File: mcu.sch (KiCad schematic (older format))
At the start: 31 parts, among them J4 UEXT, P1 CONN_01X02, SW2 SW_PUSH, T3 MMBT3904, U2 STM32F072CB, U6 24AA01, Y1 8MHz

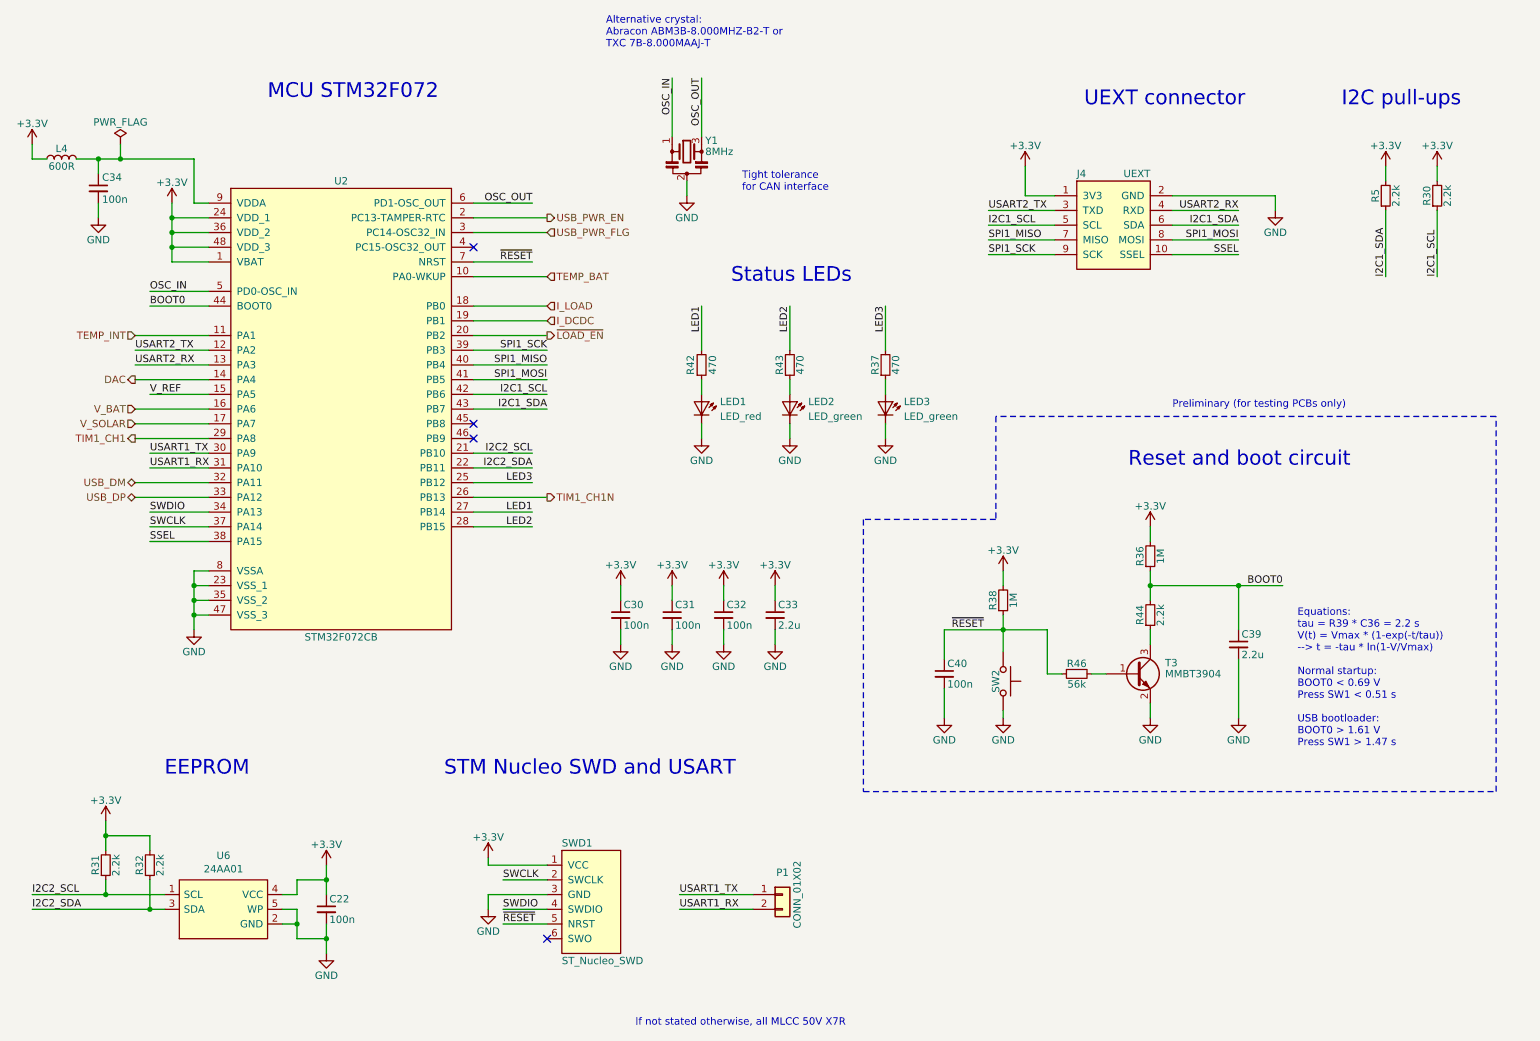
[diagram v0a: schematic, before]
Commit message: Several improvements (v0.4) after first tests
- Ultra-low-power MCU STM32L072
- Larger screw terminals
- USB power supply replaced by more efficient SMPS
- High-side load switch with P-MOS
- High-side current measurement to include USB current in load measurement
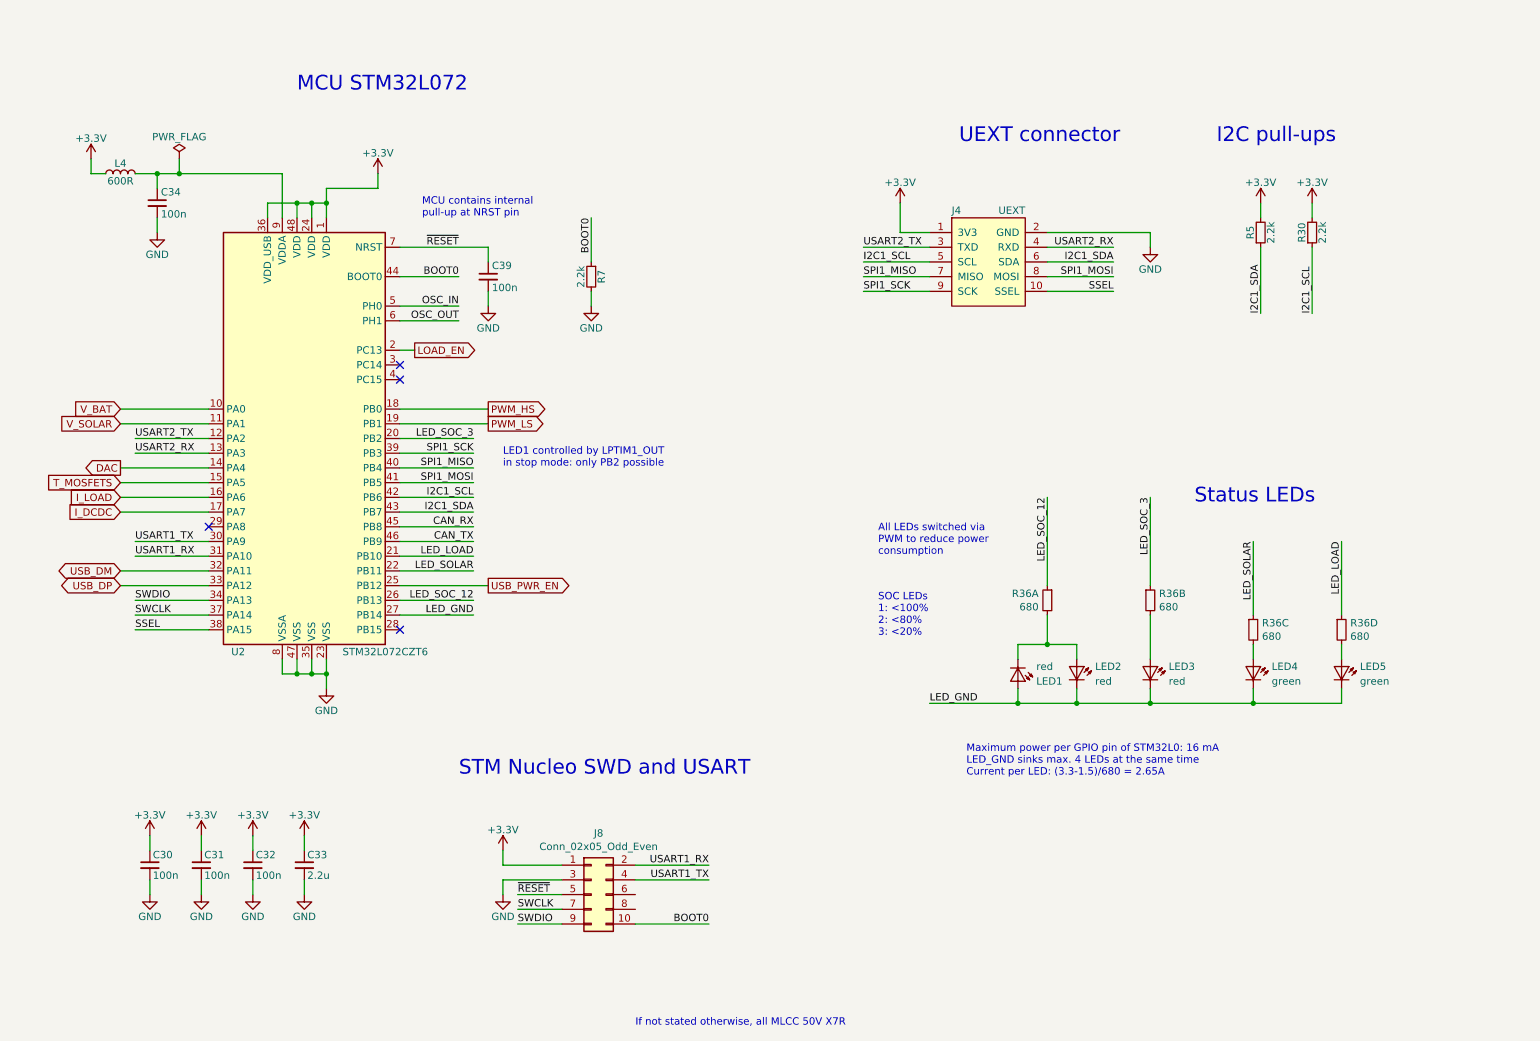
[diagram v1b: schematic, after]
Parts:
- removed C22, C40: 100n, LibreSolar:C_0603_1608, symbol Project:C
- removed P1: CONN_01X02, Connector_PinHeader_2.54mm:PinHeader_1x02_P2.54mm_Vertical, symbol Connector_Generic:Conn_01x02
- removed R31, R32, R44: 2.2k, LibreSolar:R_0603_1608, symbol Project:R
- removed R36, R38: 1M, LibreSolar:R_0603_1608, symbol Project:R
- removed R37, R42, R43: 470, LibreSolar:R_0603_1608, symbol Project:R
- removed R46: 56k, LibreSolar:R_0603_1608, symbol Project:R
- removed SW2: SW_PUSH, LibreSolar:SW_SPST_6mm, symbol Switch:SW_Push
- removed SWD1: ST_Nucleo_SWD, Connector_PinHeader_2.54mm:PinHeader_1x06_P2.54mm_Vertical, symbol Project:ST_Nucleo_SWD
- removed T3: MMBT3904, LibreSolar:SOT-23, symbol Transistor_BJT:BC817
- removed U2: STM32F072CB, Package_QFP:LQFP-48_7x7mm_P0.5mm, symbol Project:STM32F072CB
- removed U6: 24AA01, LibreSolar:SOT-23-5, symbol Project:24AA01
- removed Y1: 8MHz, LibreSolar:Resonator_Murata_CSTCE_G, symbol Device:Resonator_Small
- added J8: Conn_02x05_Odd_Even, Connector_PinHeader_2.54mm:PinHeader_2x05_P2.54mm_Vertical, symbol Connector_Generic:Conn_02x05_Odd_Even
- added LED2, LED3: red, LED_SMD:LED_0603_1608Metric, symbol Project:D_LED
- added R36: 680, LibreSolar:R_Array_Convex_4x0603, symbol Project:R_Array_4
- added R7: 2.2k, LibreSolar:R_0603_1608, symbol Project:R
- added U2: STM32L072CZT6, Package_QFP:LQFP-48_7x7mm_P0.5mm, symbol MCU_ST_STM32L0:STM32L072CZTx
- C39: value 2.2u -> 100n; Manufacturer Murata -> Yageo; PartNumber GRM188R61E225KA12D -> CC0603KRX7R9BB104; Remarks 25V, X5R -> (none)
- LED1: value LED_red -> red; Remarks red -> (none)
- LED2: value LED_green -> green; PartNumber LTST-C190GKT -> LTST-C190KGKT
- LED5: renamed from LED3; value LED_green -> green; PartNumber LTST-C190GKT -> LTST-C190KGKT
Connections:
- net +3V3: now also J8.1 (Pin_1), U2.1 (VDD), U2.24 (VDD), U2.36 (VDD_USB), U2.48 (VDD)
- net BOOT0: now also J8.10 (Pin_10), R7.1, U2.44 (BOOT0); no longer C39.1
- net DAC: now also U2.14 (PA4)
- net GND: now also J8.3 (Pin_3), R7.2, U2.23 (VSS), U2.35 (VSS), U2.47 (VSS), U2.8 (VSSA); no longer LED1.1 (K), LED2.1 (K), LED5.1 (K)
- net I2C1_SCL: now also U2.42 (PB6)
- net I2C1_SDA: now also U2.43 (PB7)
- net I_DCDC: now also U2.17 (PA7)
- net I_LOAD: now also U2.16 (PA6)
- net OSC_IN: now also U2.5 (PH0)
- net OSC_OUT: now also U2.6 (PH1)
- net SPI1_MISO: now also U2.40 (PB4)
- net SPI1_MOSI: now also U2.41 (PB5)
- net SPI1_SCK: now also U2.39 (PB3)
- net SSEL: now also U2.38 (PA15)
- net SWCLK: now also J8.7 (Pin_7), U2.37 (PA14)
- net SWDIO: now also J8.9 (Pin_9), U2.34 (PA13)
- net USART1_RX: now also J8.2 (Pin_2), U2.31 (PA10)
- net USART1_TX: now also J8.4 (Pin_4), U2.30 (PA9)
- net USART2_RX: now also U2.13 (PA3)
- net USART2_TX: now also U2.12 (PA2)
- net USB_DM: now also U2.32 (PA11)
- net USB_DP: now also U2.33 (PA12)
- net USB_PWR_EN: now also U2.25 (PB12)
- net V_BAT: now also U2.10 (PA0)
- net V_SOLAR: now also U2.11 (PA1)
- net ~RESET: now also C39.1, J8.5 (Pin_5), U2.7 (NRST)
- net at C34.1, L4.2: now also U2.9 (VDDA)
- net LED_GND: now reaches LED1.2 (A)
- net LED_GND: now also LED2.1 (K), LED5.1 (K), LED2.1 (K), LED3.1 (K), U2.27 (PB14)
- net at LED2.2 (A): now also R36.6
- net at LED5.2 (A): now also R36.8
- new net: LED1.1 (K), LED2.2 (A), R36.2
- new net: LED3.2 (A), R36.4
- new net CAN_RX: U2.45 (PB8)
- new net CAN_TX: U2.46 (PB9)
- new net LED_LOAD: R36.7, U2.21 (PB10)
- new net LED_SOC_12: R36.1, U2.26 (PB13)
- new net LED_SOC_3: R36.3, U2.20 (PB2)
- new net LED_SOLAR: R36.5, U2.22 (PB11)
- new net LOAD_EN: U2.2 (PC13)
- new net PWM_HS: U2.18 (PB0)
- new net PWM_LS: U2.19 (PB1)
- new net T_MOSFETS: U2.15 (PA5)
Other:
- note added: "All LEDs switched via\nPWM to reduce power\nconsumption"
- note added: "LED1 controlled by LPTIM1_OUT\nin stop mode: only PB2 possible"
- note added: "MCU STM32L072"
- note added: "MCU contains internal\npull-up at NRST pin"
- note added: "Maximum power per GPIO pin of STM32L0: 16 mA\nLED_GND sinks max. 4 LEDs at the same time\nCurrent per LED: (3.3-1.5)/680 = 2.65A"
- note added: "SOC LEDs\n1: <100%\n2: <80%\n3: <20%"
- note removed: "Alternative crystal: \nAbracon ABM3B-8.000MHZ-B2-T or\nTXC 7B-8.000MAAJ-T"
- note removed: "EEPROM"
- note removed: "Equations:\ntau = R39 * C36 = 2.2 s\nV(t) = Vmax * (1-exp(-t/tau))\n--> t = -tau * ln(1-V/Vmax)\n\nNormal startup:\nBOOT0 < 0.69 V\nPress SW1 < 0.51 s\n\nUSB bootloader:\nBOOT0 > 1.61 V\nPress SW1 > 1.47 s"
- note removed: "MCU STM32F072"
- note removed: "Preliminary (for testing PCBs only)"
- note removed: "Reset and boot circuit"
- note removed: "Tight tolerance\nfor CAN interface"
- moved on the sheet: C30, C31, C32, C33, C34, J4, L4, LED4, LED5, R30, R5

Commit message: Board shape adjusted and 6P6C connector added
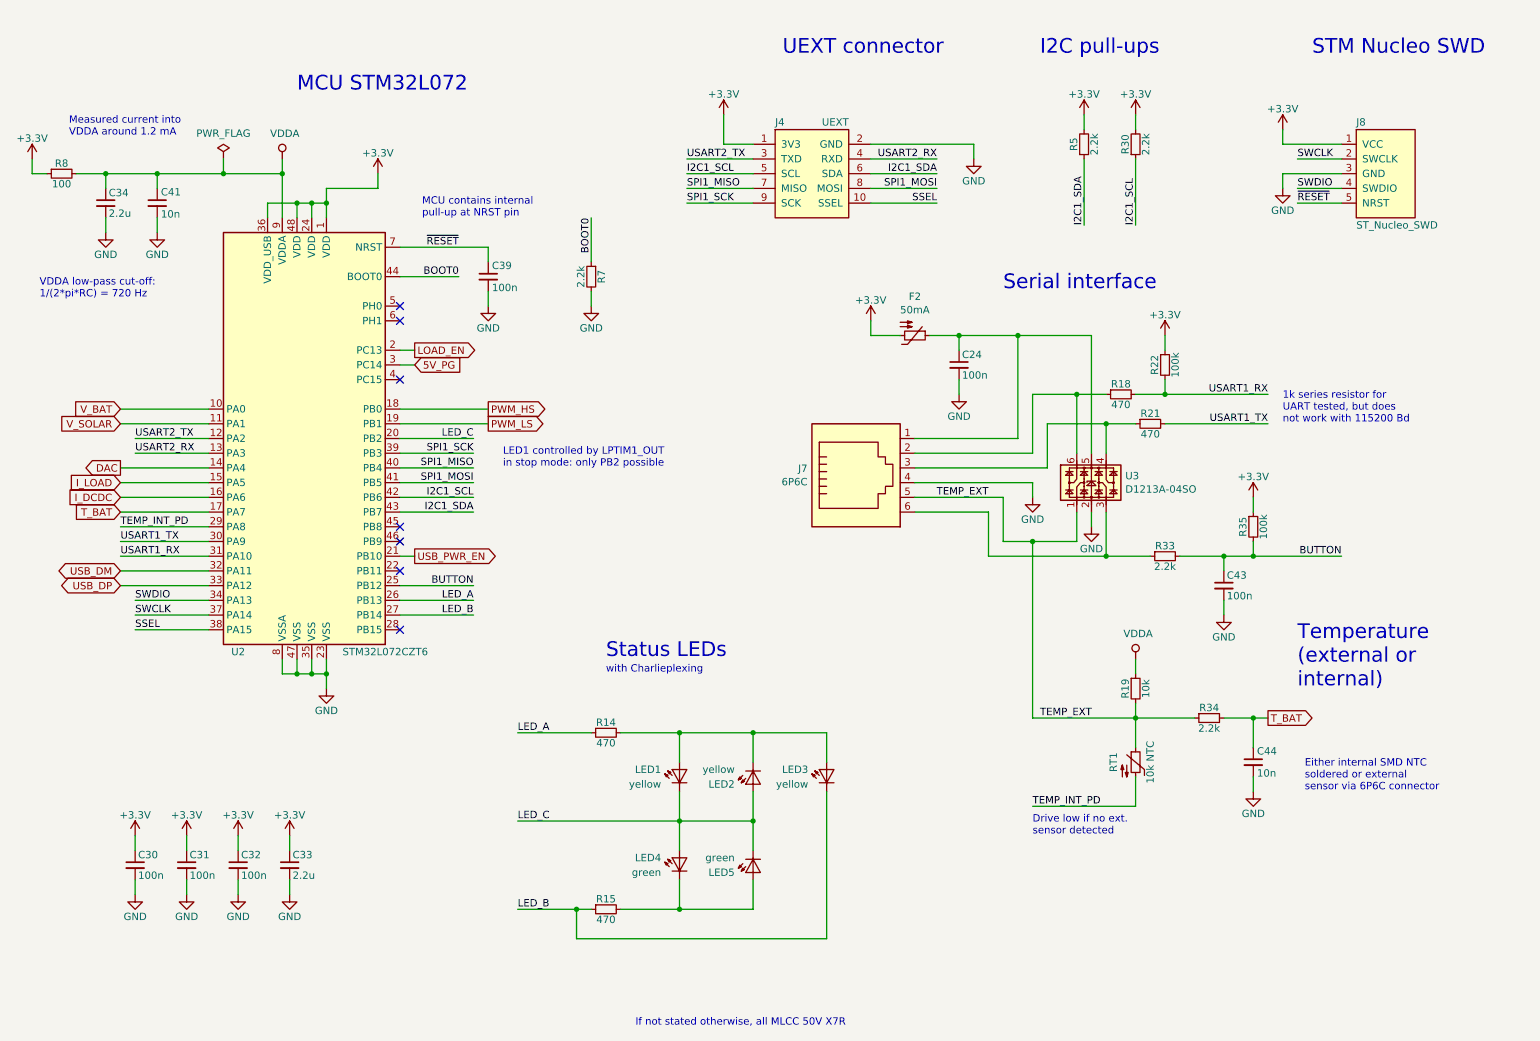
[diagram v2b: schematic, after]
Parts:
- removed J8: Conn_02x05_Odd_Even, Connector_PinHeader_2.54mm:PinHeader_2x05_P2.54mm_Vertical, symbol Connector_Generic:Conn_02x05_Odd_Even
- removed L4: 600R, Inductor_SMD:L_0603_1608Metric, symbol Project:L
- removed LED2: green, LED_SMD:LED_0603_1608Metric, symbol Project:D_LED
- removed LED2: red, LED_SMD:LED_0603_1608Metric, symbol Project:D_LED
- removed R36: 680, LibreSolar:R_Array_Convex_4x0603, symbol Project:R_Array_4
- added C24, C43: 100n, LibreSolar:C_0603_1608, symbol Project:C
- added C41, C44: 10n, LibreSolar:C_0603_1608, symbol Project:C
- added F2: 50mA, LibreSolar:R_1206_3216, symbol Project:R_PTC
- added J7: 6P6C, LibreSolar:RJ25_6P6C_TabUp, symbol Connector:6P6C
- added J8: ST_Nucleo_SWD, Connector_PinHeader_2.54mm:PinHeader_1x05_P2.54mm_Vertical, symbol Project:ST_Nucleo_SWD_5p
- added LED2: green, LibreSolar:LED_0603_D3.0mm, symbol Project:D_LED
- added LED2: yellow, LibreSolar:LED_0603_D3.0mm, symbol Project:D_LED
- added R14, R15, R18, R21: 470, LibreSolar:R_0603_1608, symbol Project:R
- added R19: 10k, LibreSolar:R_0603_1608, symbol Project:R
- added R22, R35: 100k, LibreSolar:R_0603_1608, symbol Project:R
- added R33, R34: 2.2k, LibreSolar:R_0603_1608, symbol Project:R
- added R8: 100, LibreSolar:R_0603_1608, symbol Project:R
- added RT1: 10k NTC, LibreSolar:R_0603_1608, symbol LibreSolar:R_NTC
- added U3: D1213A-04SO, LibreSolar:SOT-23-6, symbol Power_Protection:NUP4202
- C34: value 100n -> 2.2u; Manufacturer Yageo -> Murata; PartNumber CC0603KRX7R9BB104 -> GRM188R61E225KA12D; Remarks (none) -> 25V, X5R
- J4: Manufacturer (none) -> On Shore Technology Inc.; PartNumber (none) -> 302-S101
- LED1, LED3: value red -> yellow; footprint LED_SMD:LED_0603_1608Metric -> LibreSolar:LED_0603_D3.0mm; PartNumber LTST-C190KRKT -> LTST-C191KSKT; Remarks (none) -> Alternative: LTL-1CHY (3mm THT)
- LED5: footprint LED_SMD:LED_0603_1608Metric -> LibreSolar:LED_0603_D3.0mm; Remarks (none) -> Alternative: LTL-4231 (3mm THT)
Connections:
- net LED_LOAD is gone; now on net USB_PWR_EN: U2.21 (PB10)
- net LED_SOC_3 is gone; now on net LED_C: U2.20 (PB2)
- net T_MOSFETS is gone; now on net I_LOAD: U2.15 (PA5)
- net +3V3: now also F2.2, J8.1 (VCC), R22.1, R35.1, R8.1
- net GND: now also C24.2, C41.2, C43.2, C44.2, J7.4, J8.3 (GND), U3.2
- net I_DCDC: now also U2.16 (PA6); no longer U2.17 (PA7)
- net I_LOAD: no longer U2.16 (PA6)
- net SWCLK: now also J8.2 (SWCLK)
- net SWDIO: now also J8.4 (SWDIO)
- net USART1_RX: now also R18.2, R22.2
- net USART1_TX: now also R21.2
- net USB_PWR_EN: no longer U2.25 (PB12)
- net ~RESET: now also J8.5 (NRST)
- net VDDA: now reaches C34.1, U2.9 (VDDA)
- net VDDA: now also C41.1, R19.1, R8.2
- net at LED5.2 (A): now also LED2.1 (K), R15.2
- net LED_C: now reaches LED1.1 (K)
- net LED_C: now also LED5.1 (K), LED2.2 (A), LED2.2 (A)
- net at LED3.2 (A): now also LED1.2 (A), LED2.1 (K), R14.2
- net TEMP_INT_PD: now reaches U2.29 (PA8)
- net TEMP_INT_PD: now also RT1.2
- net 5V_PG: now reaches U2.3 (PC14)
- net CAN_RX: no longer names the net of U2.45 (PB8)
- net CAN_TX: no longer names the net of U2.46 (PB9)
- net LED_GND renamed LED_B
- net LED_B: now also R15.1; no longer LED1.2 (A), LED5.1 (K)
- net LED_SOC_12 renamed LED_A
- net LED_A: now also R14.1
- net LED_SOLAR: no longer names the net of U2.22 (PB11)
- net OSC_IN: no longer names the net of U2.5 (PH0)
- net OSC_OUT: no longer names the net of U2.6 (PH1)
- new net: C24.1, F2.1, J7.1, U3.5
- new net: J7.2, R18.1, U3.6
- new net: J7.3, R21.1, U3.4
- new net: J7.6, R33.1, U3.3
- new net BUTTON: C43.1, R33.2, R35.2, U2.25 (PB12)
- new net TEMP_EXT: J7.5, R19.2, R34.1, RT1.1, U3.1
- new net T_BAT: C44.1, R34.2, U2.17 (PA7)
- no-connect marks 4 -> 7
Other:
- note added: "1k series resistor for\nUART tested, but does \nnot work with 115200 Bd"
- note added: "Drive low if no ext. \nsensor detected"
- note added: "Either internal SMD NTC\nsoldered or external \nsensor via 6P6C connector"
- note added: "Measured current into\nVDDA around 1.2 mA"
- note added: "STM Nucleo SWD"
- note added: "Serial interface"
- note added: "Temperature\n(external or \ninternal)"
- note added: "VDDA low-pass cut-off:\n1/(2*pi*RC) = 720 Hz"
- note added: "with Charlieplexing"
- note removed: "All LEDs switched via\nPWM to reduce power\nconsumption"
- note removed: "Maximum power per GPIO pin of STM32L0: 16 mA\nLED_GND sinks max. 4 LEDs at the same time\nCurrent per LED: (3.3-1.5)/680 = 2.65A"
- note removed: "SOC LEDs\n1: <100%\n2: <80%\n3: <20%"
- note removed: "STM Nucleo SWD and USART"
- moved on the sheet: C30, C31, J4, LED1, LED3, LED5

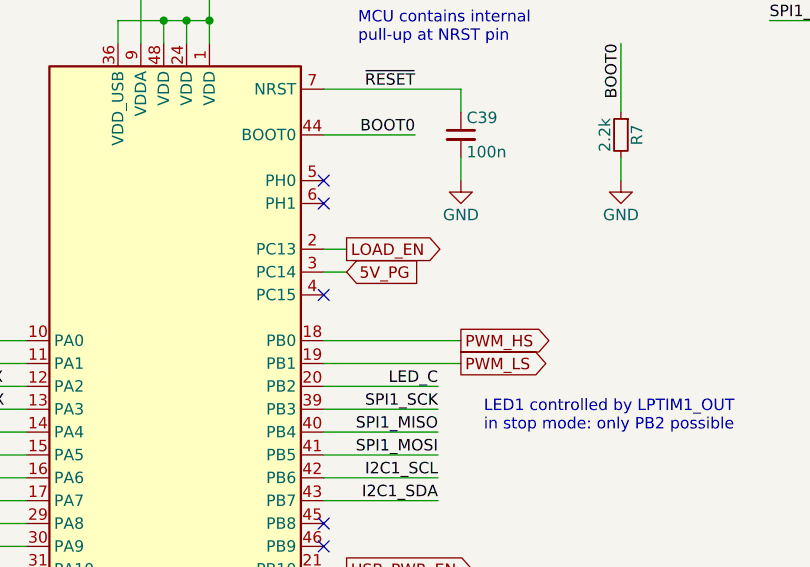
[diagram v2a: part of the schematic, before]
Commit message: Solar voltage input protection added
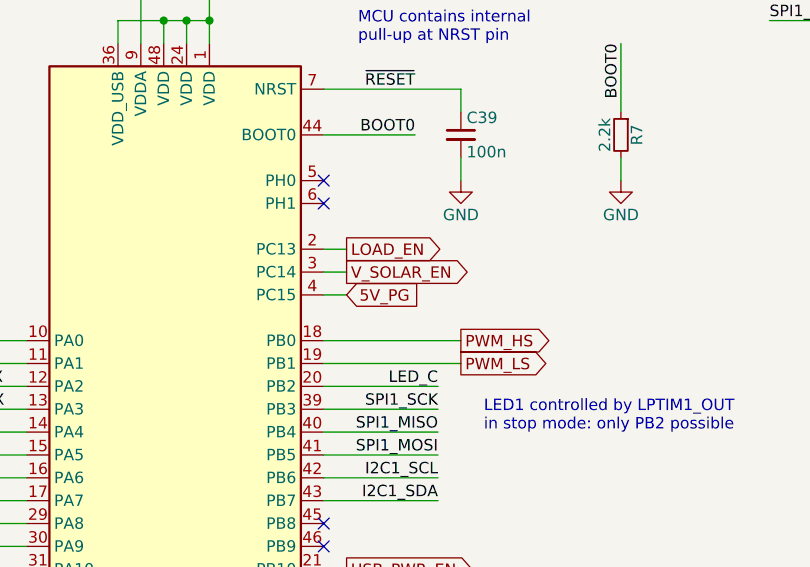
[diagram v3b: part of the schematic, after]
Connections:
- net 5V_PG: now also U2.4 (PC15); no longer U2.3 (PC14)
- new net V_SOLAR_EN: U2.3 (PC14)
- no-connect marks 7 -> 6
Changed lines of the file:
@@
 EESchema Schematic File Version 4
-LIBS:mptt-10a-cache
+LIBS:mppt-10a-cache
 EELAYER 29 0
 EELAYER END
@@
 Sheet 3 4
 Title "10A MPPT Charge Controller with USB"
-Date "2019-03-24"
-Rev "0.5"
+Date "2019-04-09"
+Rev "0.6"
 Comp "Libre Solar / Connected Energy"
 Comment1 "Author: Martin Jäger"
@@
 Wire Wire Line
 	2200 3900 1600 3900
-NoConn ~ 3500 3200
 Wire Wire Line
 	2200 4000 1600 4000
@@
 Wire Wire Line
 	3500 3100 3600 3100
-Text GLabel 3600 3100 2    50   Input ~ 0
+Text GLabel 3600 3200 2    50   Input ~ 0
 5V_PG
+Text GLabel 3600 3100 2    50   Output ~ 0
+V_SOLAR_EN
+Wire Wire Line
+	3600 3200 3500 3200
 $EndSCHEMATC
